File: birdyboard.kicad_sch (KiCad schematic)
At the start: 15 parts, among them J0 24V Input Screw Terminal, J1 JST-PH StepMotor Conn, J2 JST-PH StepMotor Conn, J3 JST-PH StepMotor Conn, J4 JST-PH StepMotor Conn, J5 AS5047_Adapter_Board_Connector, J6 AS5047_Adapter_Board_Connector, J7 AS5047_Adapter_Board_Connector, J8 AS5047_Adapter_Board_Connector, U0 TMC2208_SILENTSTEPSTICK, U1 TMC2208_SILENTSTEPSTICK, U2 TMC2208_SILENTSTEPSTICK, U3 TMC2208_SILENTSTEPSTICK, U5 Pico, U6 SN74CBT3253 MUX/DEMUX

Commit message: fix broken trace
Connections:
- net +24V: now also J0.24V (Pin_1)
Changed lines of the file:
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@@
+    (stroke (width 0) (type default) (color 0 0 0 0))
+  )
+  (wire (pts (xy 20.32 95.25) (xy 24.13 95.25))
     (stroke (width 0) (type default) (color 0 0 0 0))
   )
@@
     (stroke (width 0) (type default) (color 0 0 0 0))
   )
+  (wire (pts (xy 20.32 92.71) (xy 20.32 95.25))
+    (stroke (width 0) (type default) (color 0 0 0 0))
+  )

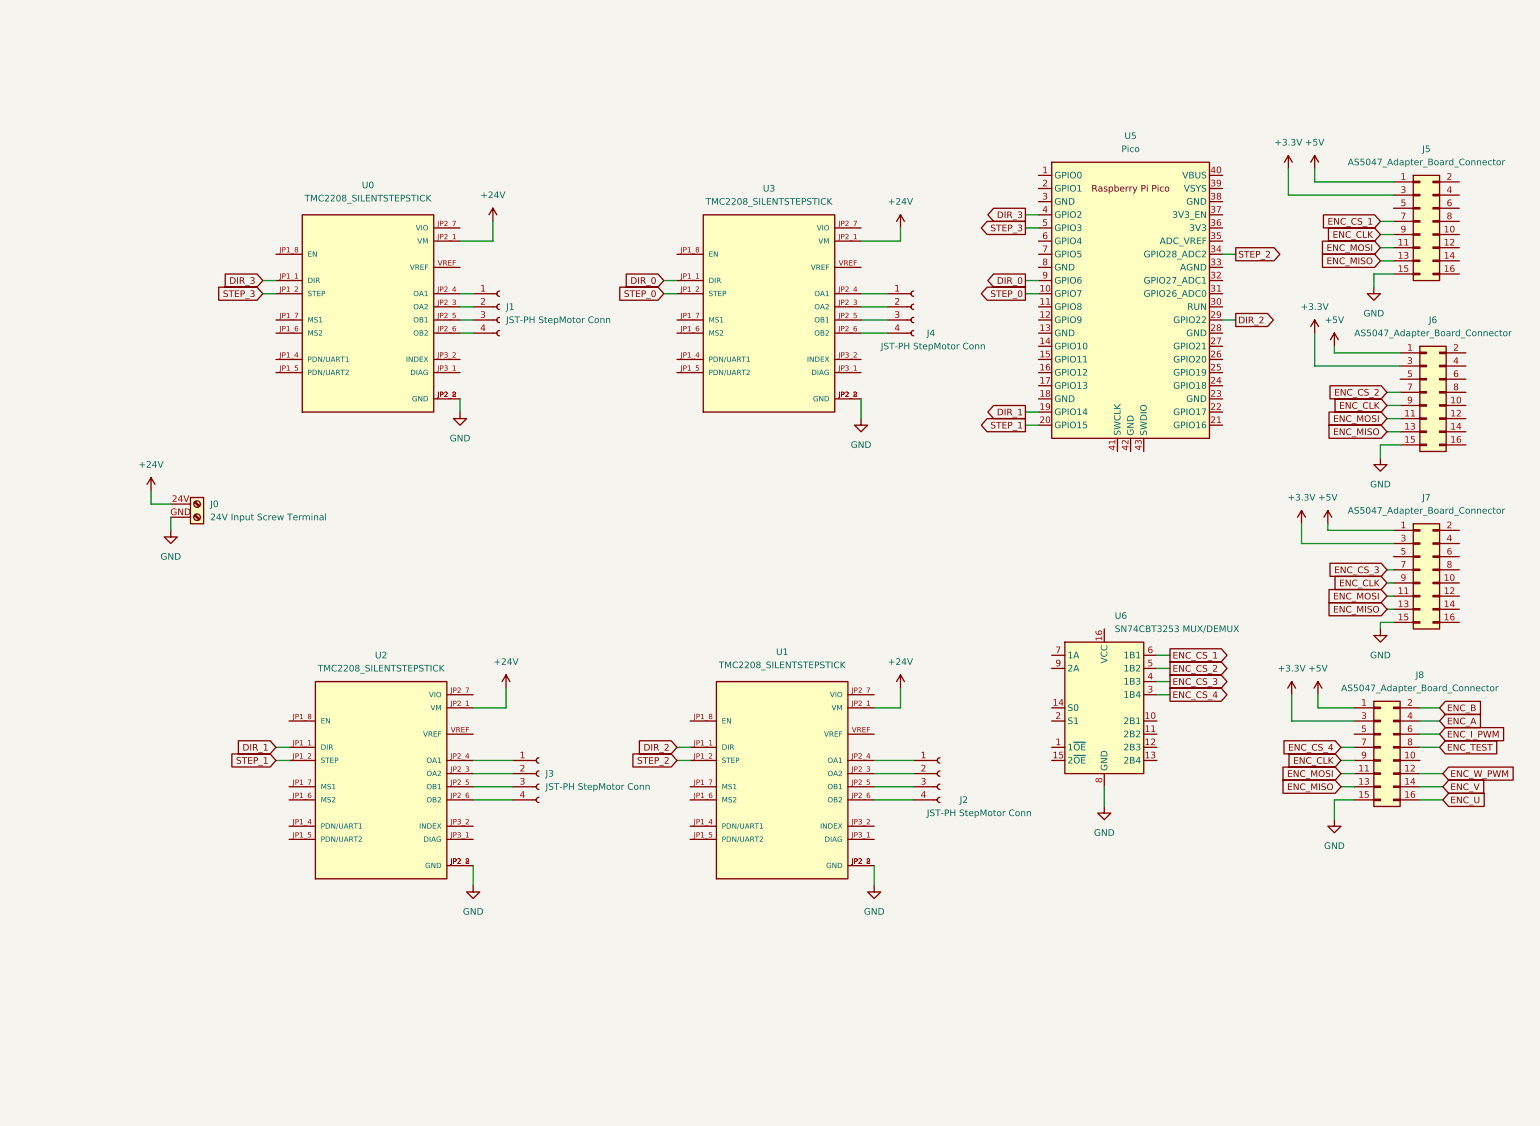
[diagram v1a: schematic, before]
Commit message: Adds 24-5v & 3.3v converters
-- adds 3d model for TMC2209 stepsticks
-- adds extra screw-terminal type connectors for stepper motors
-- adds a jumper to allow a single encoder to run without installing a mux
-- adds ENC_CS connections
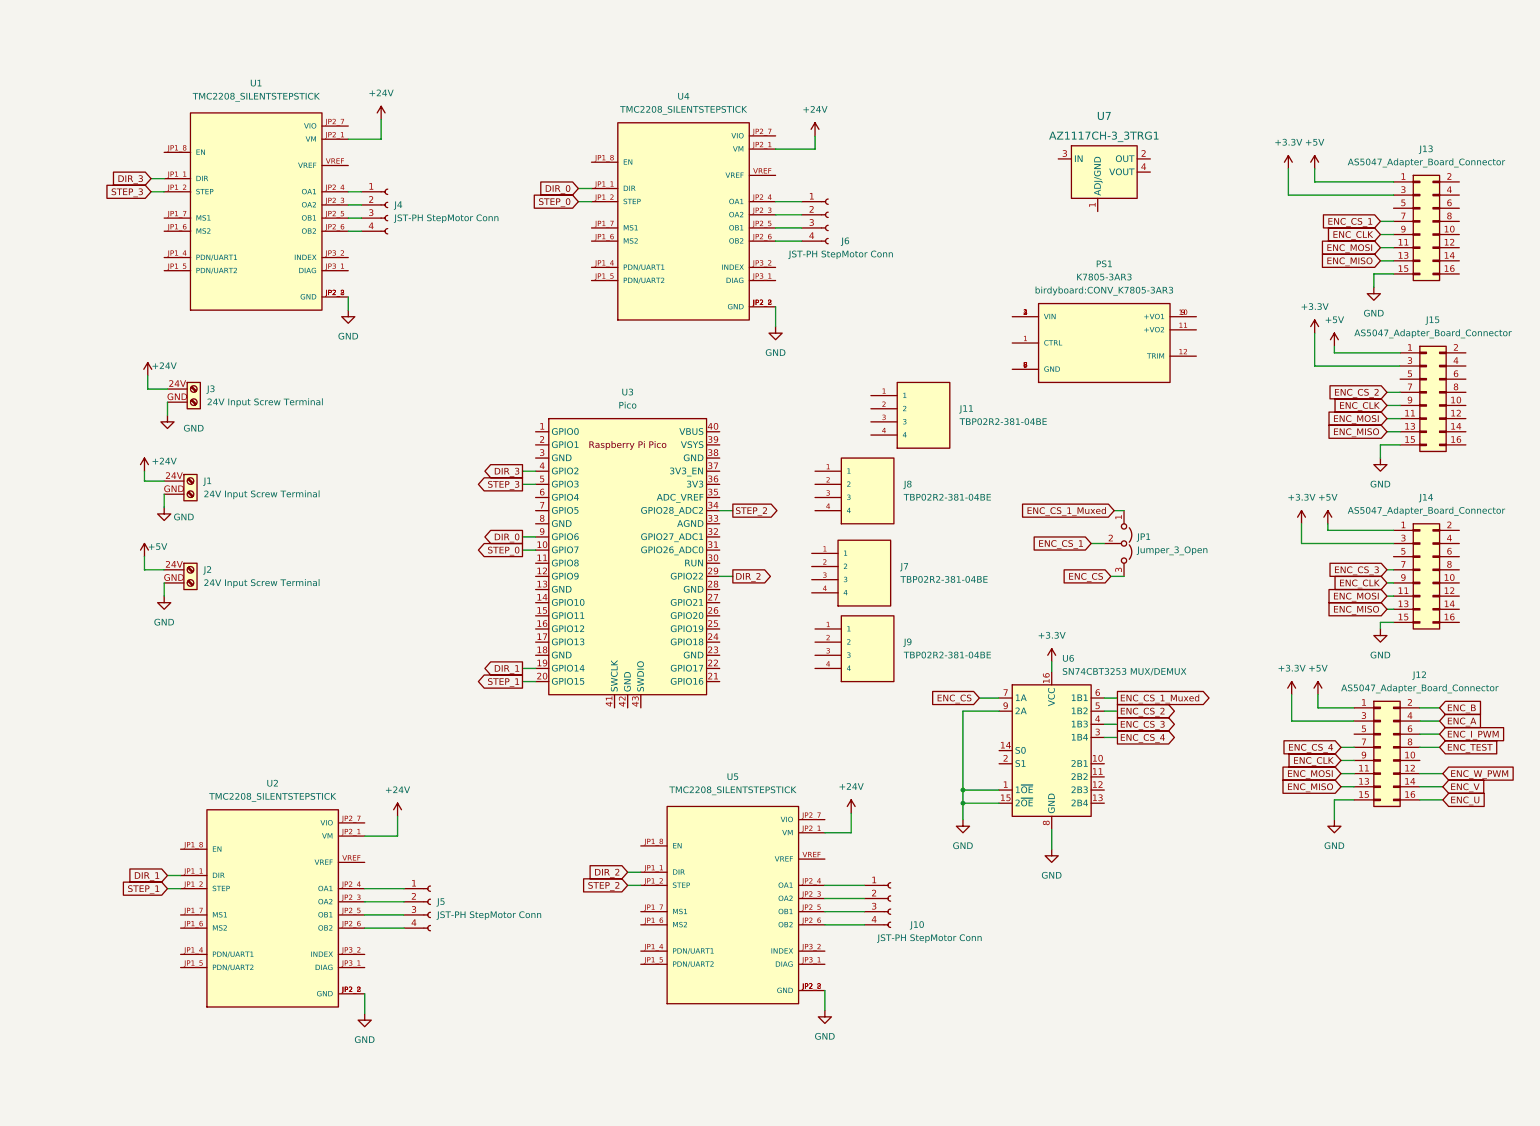
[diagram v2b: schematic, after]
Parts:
- added J11, J7, J8, J9: TBP02R2-381-04BE, birdyboard:CUI_TBP02R2-381-04BE, symbol birdyboard_library:TBP02R2-381-04BE
- added J2, J3: 24V Input Screw Terminal, birdyboard:CUI_TBP01R2-508-02BE, symbol Connector:Screw_Terminal_01x02
- added JP1: Jumper_3_Open, symbol Jumper:Jumper_3_Open
- added PS1: K7805-3AR3, birdyboard:CONV_K7805-3AR3, symbol birdyboard_library:K7805-3AR3
- added U7: AZ1117CH-3_3TRG1, digikey-footprints:SOT-223, symbol dk_PMIC-Voltage-Regulators-Linear:AZ1117CH-3_3TRG1
- J10: renamed from J2; footprint (none) -> Connector_JST:JST_XH_B4B-XH-A_1x04_P2.50mm_Vertical
- J4: renamed from J1; footprint (none) -> Connector_JST:JST_XH_B4B-XH-A_1x04_P2.50mm_Vertical
- J5: renamed from J3; footprint (none) -> Connector_JST:JST_XH_B4B-XH-A_1x04_P2.50mm_Vertical
- J6: renamed from J4; footprint (none) -> Connector_JST:JST_XH_B4B-XH-A_1x04_P2.50mm_Vertical
- renumbered J0 to J1, J8 to J12, J5 to J13, J7 to J14, J6 to J15, U0 to U1, U5 to U3, U3 to U4, U1 to U5
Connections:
- net +24V: now also J3.24V (Pin_1)
- net +3V3: now also U6.16 (VCC)
- net +5V: now also J2.24V (Pin_1)
- net ENC_CS_1: now also JP1.2 (C); no longer U6.6 (1B1)
- net GND: now also U6.1 (1~{OE}), U6.15 (2~{OE}), U6.9 (2A), J2.GND (Pin_2), J3.GND (Pin_2)
- net ENC_CS: now reaches U6.7 (1A)
- net ENC_CS: now also JP1.3 (B)
- new net: PS1.10 (+VO1), PS1.9 (+VO1)
- new net: PS1.2 (VIN), PS1.3 (VIN), PS1.4 (VIN)
- new net: PS1.5 (GND), PS1.6 (GND), PS1.7 (GND), PS1.8 (GND)
- new net ENC_CS_1_Muxed: JP1.1 (A), U6.6 (1B1)
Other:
- moved on the sheet: J1, J10, J4, J5, J6, U1, U2, U3, U4, U5, U6

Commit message: Completes TMC2209 & PSU circuits
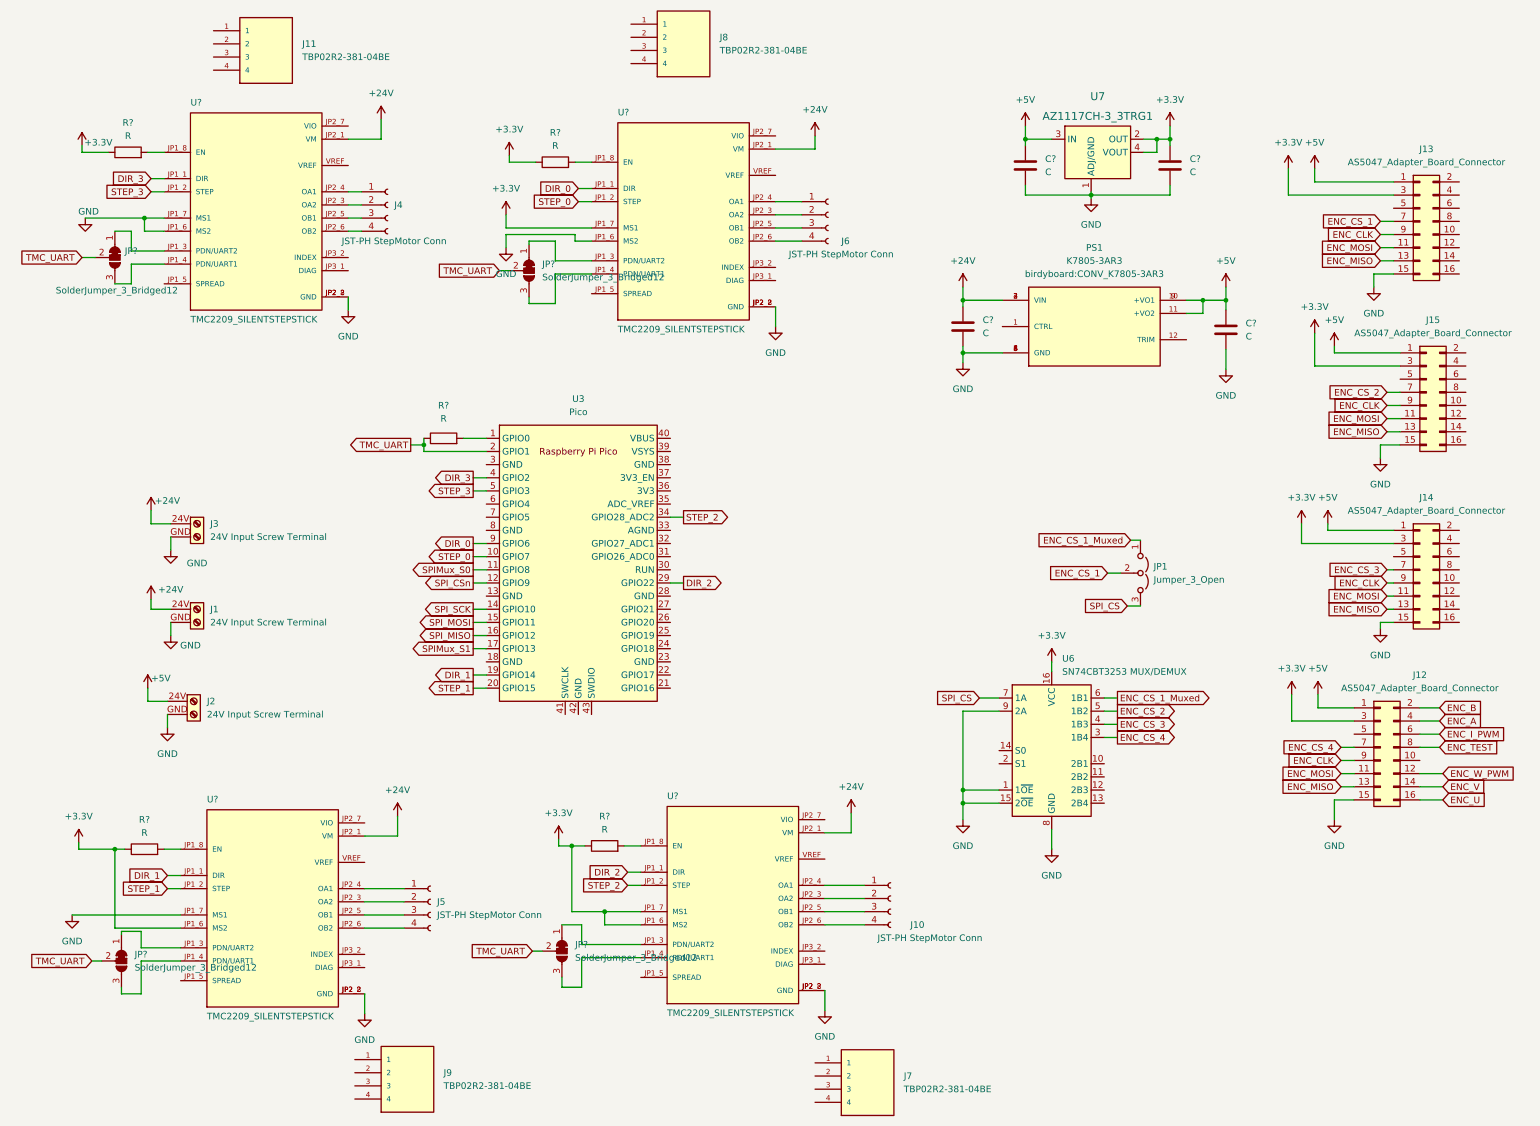
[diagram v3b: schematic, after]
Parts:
- added C? (x4): C, symbol Device:C
- added JP? (x4): SolderJumper_3_Bridged12, symbol Jumper:SolderJumper_3_Bridged12
- added R? (x5): R, symbol Device:R
- U?: renamed from U4; value TMC2208_SILENTSTEPSTICK -> TMC2209_SILENTSTEPSTICK; footprint birdyboard:TMC2208_SILENTSTEPSTICK -> MODULE_TMC2208_SILENTSTEPSTICK; symbol birdyboard_library:TMC2208_SILENTSTEPSTICK -> birdyboard_library:TMC2209_SILENTSTEPSTICK
- U?: renamed from U2; value TMC2208_SILENTSTEPSTICK -> TMC2209_SILENTSTEPSTICK; footprint birdyboard:TMC2208_SILENTSTEPSTICK -> MODULE_TMC2208_SILENTSTEPSTICK; symbol birdyboard_library:TMC2208_SILENTSTEPSTICK -> birdyboard_library:TMC2209_SILENTSTEPSTICK
- U?: renamed from U1; value TMC2208_SILENTSTEPSTICK -> TMC2209_SILENTSTEPSTICK; footprint birdyboard:TMC2208_SILENTSTEPSTICK -> MODULE_TMC2208_SILENTSTEPSTICK; symbol birdyboard_library:TMC2208_SILENTSTEPSTICK -> birdyboard_library:TMC2209_SILENTSTEPSTICK
- U?: renamed from U5; value TMC2208_SILENTSTEPSTICK -> TMC2209_SILENTSTEPSTICK; footprint birdyboard:TMC2208_SILENTSTEPSTICK -> MODULE_TMC2208_SILENTSTEPSTICK; symbol birdyboard_library:TMC2208_SILENTSTEPSTICK -> birdyboard_library:TMC2209_SILENTSTEPSTICK
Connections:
- net +24V: now also PS1.2 (VIN), PS1.3 (VIN), PS1.4 (VIN), C?.1
- net +3.3V: now also U7.2 (OUT), U7.4 (VOUT), C?.1
- net +3V3: now also U?.JP1_6 (MS2), U?.JP1_6 (MS2), U?.JP1_7 (MS1), U?.JP1_7 (MS1), R?.1, R?.1, R?.1, R?.1
- net +5V: now also PS1.10 (+VO1), PS1.11 (+VO2), PS1.9 (+VO1), U7.3 (IN), C?.1, C?.1
- net GND: now also PS1.5 (GND), PS1.6 (GND), PS1.7 (GND), PS1.8 (GND), U7.1 (ADJ/GND), U?.JP1_6 (MS2), U?.JP1_6 (MS2), U?.JP1_7 (MS1), U?.JP1_7 (MS1), C?.2, C?.2, C?.2, C?.2
- net at U?.JP1_4 (PDN/UART1): now also JP?.3 (B) (x4)
- net at U?.JP1_8 (EN): now also R?.2 (x4)
- net at U3.1 (GPIO0): now also R?.2
- net SPIMux_S0: now reaches U3.11 (GPIO8)
- net SPI_CSn: now reaches U3.12 (GPIO9)
- net SPI_SCK: now reaches U3.14 (GPIO10)
- net SPI_MOSI: now reaches U3.15 (GPIO11)
- net SPI_MISO: now reaches U3.16 (GPIO12)
- net SPIMux_S1: now reaches U3.17 (GPIO13)
- net TMC_UART: now reaches U3.2 (GPIO1)
- net TMC_UART: now also JP?.2 (C), JP?.2 (C), JP?.2 (C), JP?.2 (C), R?.1
- net ENC_CS renamed SPI_CS
- new net: JP?.1 (A), U?.JP1_3 (PDN/UART2) (x4)
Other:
- moved on the sheet: J1, J11, J2, J3, J7, J8, J9, JP1, PS1, U3, U7
